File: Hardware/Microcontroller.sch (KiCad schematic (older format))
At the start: 22 parts, among them J1 UPDI, J2 UART, J3 NMEA, J4 Vin, Q1 S8050, U3 ATtiny1606-S, U5 AMS1117-5.0

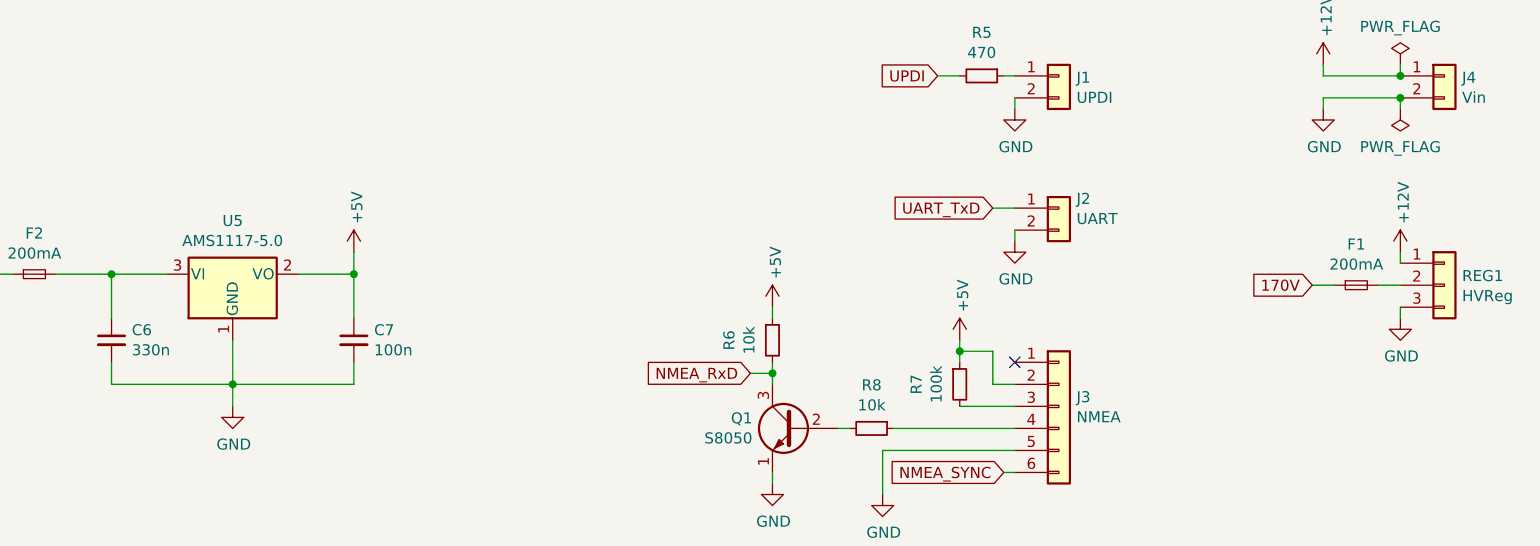
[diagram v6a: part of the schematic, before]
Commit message: Route UPDI and UART
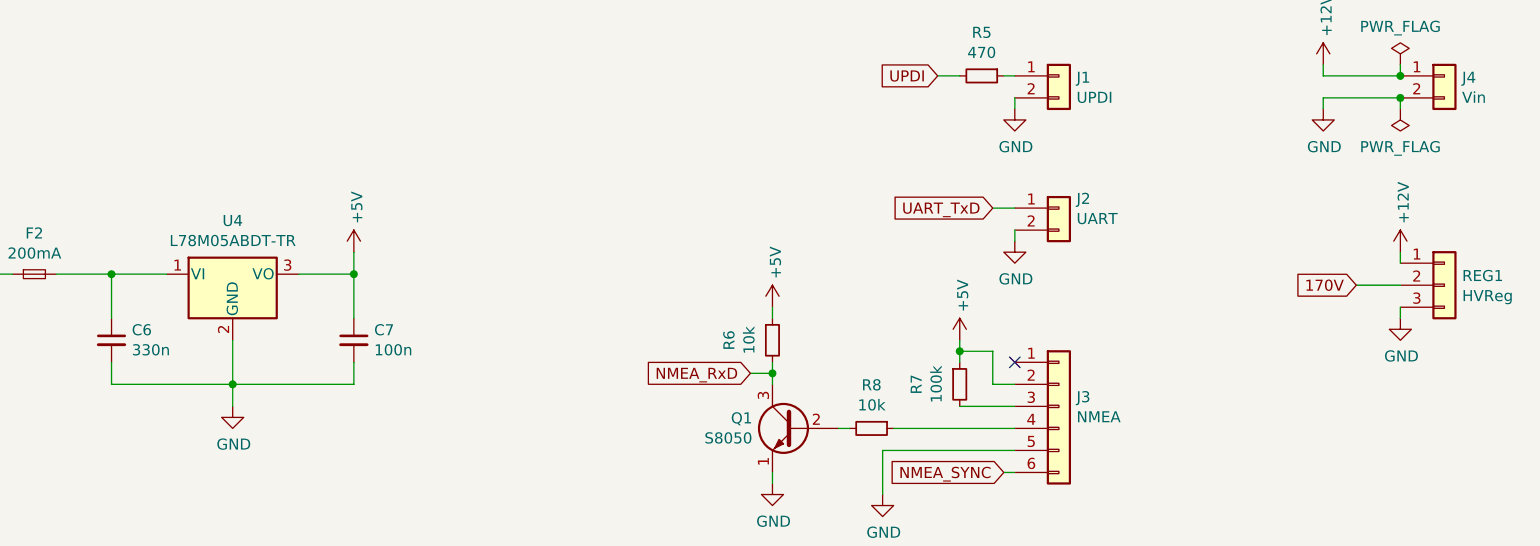
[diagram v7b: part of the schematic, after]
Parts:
- removed F1: 200mA, Fuse:Fuse_2512_6332Metric, symbol Device:Fuse_Small
- removed U5: AMS1117-5.0, Package_TO_SOT_SMD:SOT-223-3_TabPin2, symbol Regulator_Linear:AMS1117-5.0
- added U4: L78M05ABDT-TR, Package_TO_SOT_SMD:TO-252-2, symbol Regulator_Linear:LF50_TO252
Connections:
- net +5V: now also U4.3 (VO)
- net 170V: now also REG1.2 (Pin_2)
- net GND: now also U4.2 (GND)
- net at C6.1, F2.2: now also U4.1 (VI)
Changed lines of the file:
@@
 	1    0    0    -1
 $EndComp
-Text GLabel 9550 4500 0    50   Input ~ 0
+Text GLabel 9750 4500 0    50   Input ~ 0
 170V
-Wire Wire Line
-	9650 4500 9550 4500
 Wire Wire Line
 	9950 4600 9950 4650
@@
 	9950 3650 9950 3700
 Connection ~ 9950 3650
-$Comp
-L Device:Fuse_Small F1
-U 1 1 5FA2D98C
-P 9750 4500
-F 0 "F1" H 9750 4685 50  0000 C CNN
-F 1 "200mA" H 9750 4594 50  0000 C CNN
-F 2 "Fuse:Fuse_2512_6332Metric" H 9750 4500 50  0001 C CNN
-F 3 "~" H 9750 4500 50  0001 C CNN
-	1    9750 4500
-	1    0    0    -1
-$EndComp
 Wire Wire Line
 	9950 4400 9950 4350
-Wire Wire Line
-	9850 4500 9950 4500
 Wire Wire Line
 	5200 4350 5200 4450
@@
 Wire Wire Line
 	7100 4900 7100 4950
-$Comp
-L Regulator_Linear:AMS1117-5.0 U5
-U 1 1 5FA81909
+Connection ~ 4100 4450
+Wire Wire Line
+	4100 4450 4350 4450
+$Comp
+L Regulator_Linear:LF50_TO252 U4
+U 1 1 5FA94124
 P 4650 4450
-F 0 "U5" H 4650 4692 50  0000 C CNN
-F 1 "AMS1117-5.0" H 4650 4601 50  0000 C CNN
-F 2 "Package_TO_SOT_SMD:SOT-223-3_TabPin2" H 4650 4650 50  0001 C CNN
-F 3 "http://www.advanced-monolithic.com/pdf/ds1117.pdf" H 4750 4200 50  0001 C CNN
+F 0 "U4" H 4650 4692 50  0000 C CNN
+F 1 "L78M05ABDT-TR" H 4650 4601 50  0000 C CNN
+F 2 "Package_TO_SOT_SMD:TO-252-2" H 4650 4675 50  0001 C CIN
+F 3 "http://www.st.com/content/ccc/resource/technical/document/datasheet/c4/0e/7e/2a/be/bc/4c/bd/CD00000546.pdf/files/CD00000546.pdf/jcr:content/translations/en.CD00000546.pdf" H 4650 4400 50  0001 C CNN
 	1    4650 4450
 	1    0    0    -1
 $EndComp
-Connection ~ 4100 4450
-Wire Wire Line
-	4100 4450 4350 4450
+Wire Wire Line
+	9750 4500 9950 4500
 $EndSCHEMATC

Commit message: Change mounting holes to M2.5
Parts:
- H1, H2, H3, H4: footprint MountingHole:MountingHole_2.2mm_M2_Pad_Via -> MountingHole:MountingHole_2.7mm_M2.5_Pad_Via
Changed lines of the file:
@@
 F 0 "H4" V 4200 6950 50  0000 C CNN
 F 1 "Hole" V 4200 7150 50  0000 C CNN
-F 2 "MountingHole:MountingHole_2.2mm_M2_Pad_Via" H 4200 6750 50  0001 C CNN
+F 2 "MountingHole:MountingHole_2.7mm_M2.5_Pad_Via" H 4200 6750 50  0001 C CNN
 F 3 "~" H 4200 6750 50  0001 C CNN
 	1    4200 6750
@@
 F 0 "H2" V 3900 6950 50  0000 C CNN
 F 1 "Hole" V 3900 7150 50  0000 C CNN
-F 2 "MountingHole:MountingHole_2.2mm_M2_Pad_Via" H 3900 6750 50  0001 C CNN
+F 2 "MountingHole:MountingHole_2.7mm_M2.5_Pad_Via" H 3900 6750 50  0001 C CNN
 F 3 "~" H 3900 6750 50  0001 C CNN
 	1    3900 6750
@@
 F 0 "H3" V 4200 6750 50  0000 C CNN
 F 1 "Hole" V 4200 6950 50  0000 C CNN
-F 2 "MountingHole:MountingHole_2.2mm_M2_Pad_Via" H 4200 6550 50  0001 C CNN
+F 2 "MountingHole:MountingHole_2.7mm_M2.5_Pad_Via" H 4200 6550 50  0001 C CNN
 F 3 "~" H 4200 6550 50  0001 C CNN
 	1    4200 6550
@@
 F 0 "H1" V 3900 6750 50  0000 C CNN
 F 1 "Hole" V 3900 6950 50  0000 C CNN
-F 2 "MountingHole:MountingHole_2.2mm_M2_Pad_Via" H 3900 6550 50  0001 C CNN
+F 2 "MountingHole:MountingHole_2.7mm_M2.5_Pad_Via" H 3900 6550 50  0001 C CNN
 F 3 "~" H 3900 6550 50  0001 C CNN
 	1    3900 6550
